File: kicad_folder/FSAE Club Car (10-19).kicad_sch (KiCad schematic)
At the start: 19 parts, among them J1 ECU PINOUT, K1 Shutdown Relay, K2 Main Relay, K3 Fuel pump and Injectors, K4 starter control relay, K5 starter solenoid, K6 Fans Relay, SW1 BOTS, SW2 cockpit Switch, SW3 Inertia Switch, SW4 Ignition, SW5 SW_Push

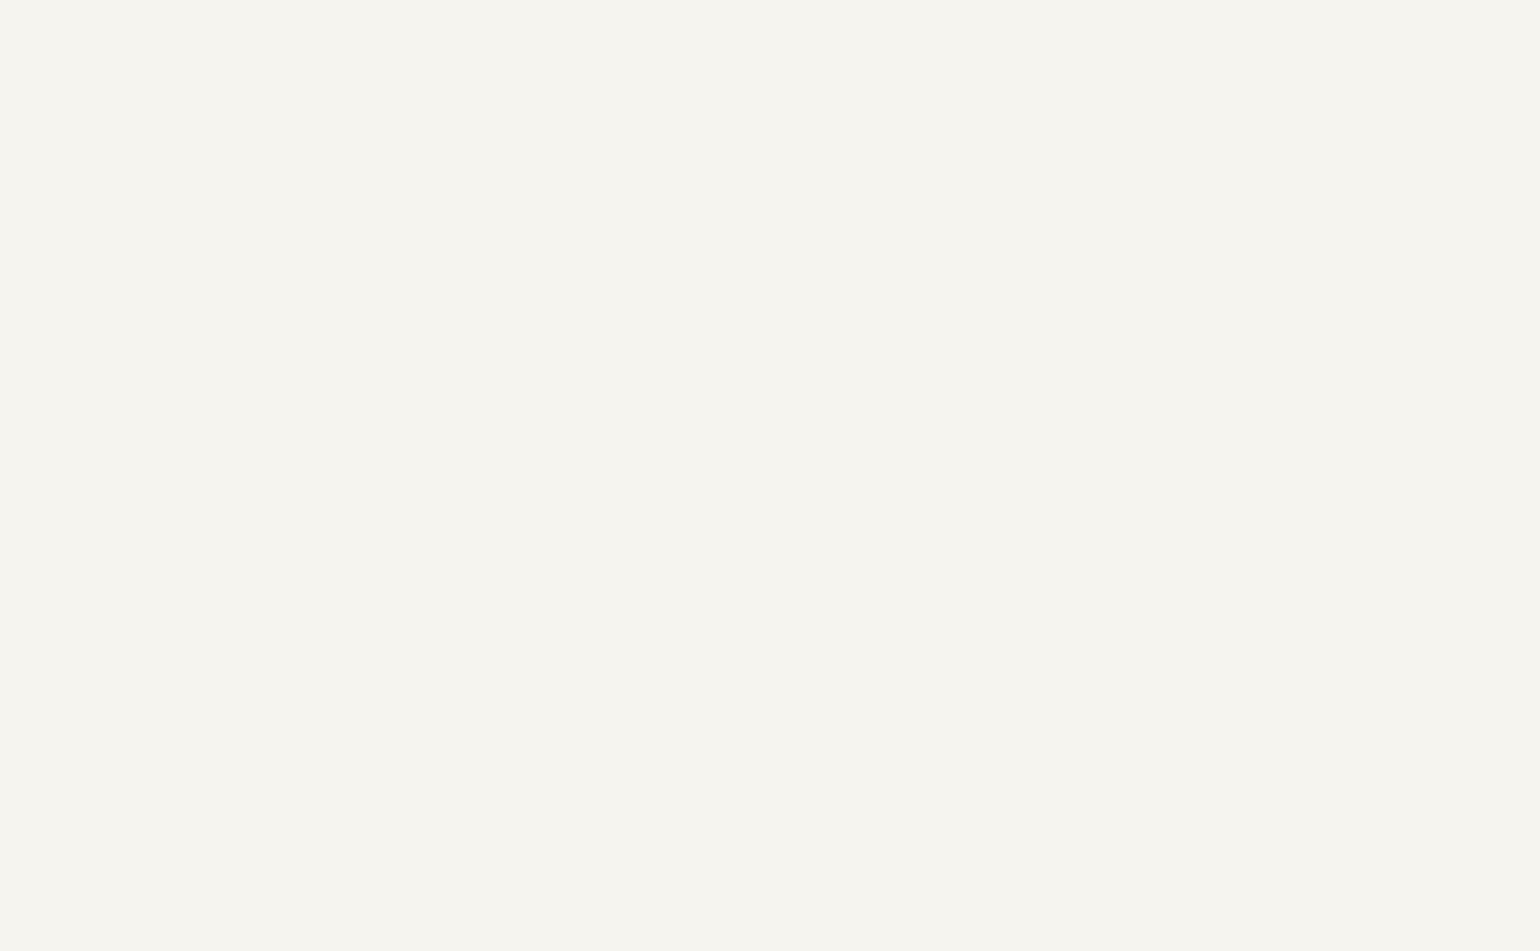
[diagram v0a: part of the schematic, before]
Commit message: redid diagram for clarity
- bots inertia switch and cockpit switch are now push open for accuracy
- starter is is now connected after ignition
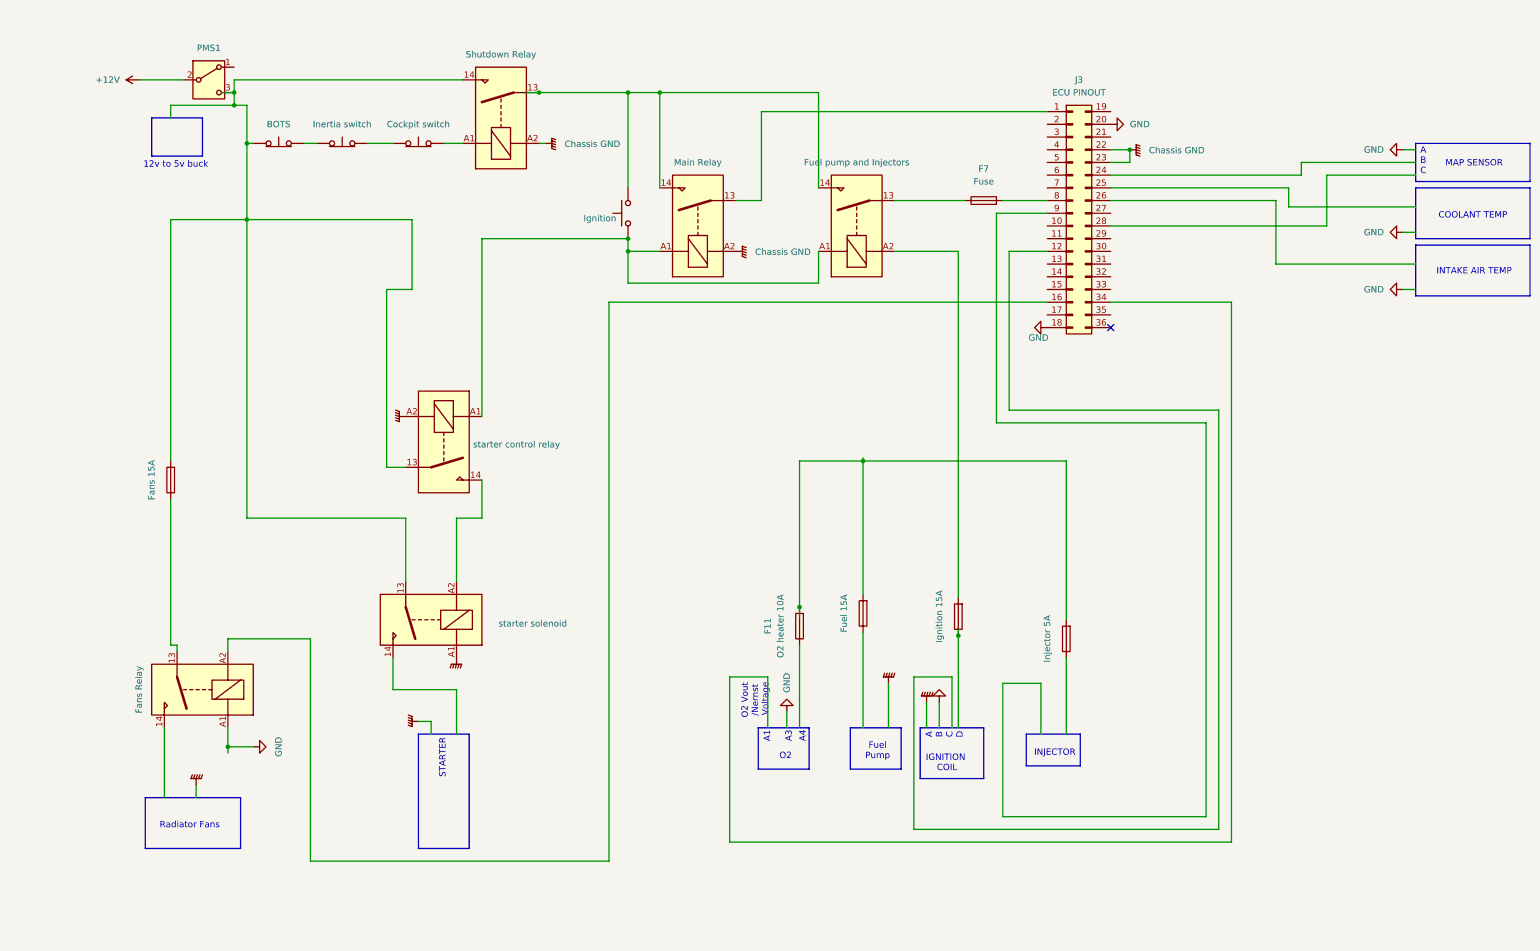
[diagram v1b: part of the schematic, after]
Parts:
- added F10: Injector 5A, symbol Device:Fuse
- added F11: O2 heater 10A, symbol Device:Fuse
- added F12: Fans 15A, symbol Device:Fuse
- added F7: Fuse, symbol Device:Fuse
- added F8: Fuel 15A, symbol Device:Fuse
- added F9: Ignition 15A, symbol Device:Fuse
- added J3: ECU PINOUT, symbol Connector_Generic:Conn_02x18_Top_Bottom
- added K10: starter control relay, Relay_THT:Relay_SPST-NO_Fujitsu_FTR-LYAA005x_FormA_Vertical, symbol Relay:Fujitsu_FTR-LYAA005x
- added K11: starter solenoid, Relay_THT:Relay_SPST-NO_Fujitsu_FTR-LYAA005x_FormA_Vertical, symbol Relay:Fujitsu_FTR-LYAA005x
- added K12: Fans Relay, Relay_THT:Relay_SPST-NO_Fujitsu_FTR-LYAA005x_FormA_Vertical, symbol Relay:Fujitsu_FTR-LYAA005x
- added K7: Shutdown Relay, Relay_THT:Relay_SPST-NO_Fujitsu_FTR-LYAA005x_FormA_Vertical, symbol Relay:Fujitsu_FTR-LYAA005x
- added K8: Main Relay, Relay_THT:Relay_SPST-NO_Fujitsu_FTR-LYAA005x_FormA_Vertical, symbol Relay:Fujitsu_FTR-LYAA005x
- added K9: Fuel pump and Injectors, Relay_THT:Relay_SPST-NO_Fujitsu_FTR-LYAA005x_FormA_Vertical, symbol Relay:Fujitsu_FTR-LYAA005x
- added PMS1: SW_SPDT, symbol Switch:SW_SPDT
- added SW10: BOTS, Button_Switch_SMD:Nidec_Copal_CAS-120A, symbol Switch:SW_Push_Open
- added SW11: Inertia switch, Button_Switch_SMD:Nidec_Copal_CAS-120A, symbol Switch:SW_Push_Open
- added SW12: Cockpit switch, Button_Switch_SMD:Nidec_Copal_CAS-120A, symbol Switch:SW_Push_Open
- added SW9: Ignition, symbol Switch:SW_Push
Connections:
- net +12V: now also PMS1.2 (B)
- net Chassis GND: now also J3.22 (Pin_22), J3.23 (Pin_23), K7.A2, K8.A2
- net GND: now also J3.18 (Pin_18), J3.20 (Pin_20), K12.A1
- net GNDPWR: now also K10.A2, K11.A1
- new net: J3.1 (Pin_1), K8.13
- new net: K7.13, K8.14, K9.14, SW9.2
- new net: K10.A1, K8.A1, K9.A1, SW9.1
- new net: J3.16 (Pin_16), K12.A2
- new net: F7.2, J3.8 (Pin_8)
- new net: F9.2, K9.A2
- new net: SW11.2 (B), SW12.1 (A)
- new net: K7.A1, SW12.2 (B)
- new net: F12.1, K12.13
- new net: F12.2, K10.13, K11.13, K7.14, PMS1.3 (C), SW10.1 (A)
- new net: K10.14, K11.A2
- new net: F10.2, F11.2, F8.2
- new net: F7.1, K9.13
- new net: SW10.2 (B), SW11.1 (A)
- no-connect marks 0 -> 1
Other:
- note added: "IGNITION COIL"
- note added: "O2 Vout /Nernst Voltage"

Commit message: stufff
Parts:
- added D1, D2, D3, D4, D5: D_Zener, Package_DIP:DIP-40_W15.24mm, symbol Device:D_Zener
- added SW13: starter, symbol Switch:SW_Push
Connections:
- net Chassis GND: now also D1.2 (A), D2.2 (A), D3.2 (A)
- net GNDPWR: now also D4.2 (A), D5.2 (A)
- net at K8.A1, K9.A1, SW9.1: now also D1.1 (K), D2.1 (K), SW13.2; no longer K10.A1
- net at J3.16 (Pin_16), K12.A2: now also D5.1 (K)
- net at F9.2: now also K9.13; no longer K9.A2
- net at K7.A1, SW12.2 (B): now also D3.1 (K)
- net at F7.1: now also K9.A2; no longer K9.13
- new net: D4.1 (K), K10.A1, SW13.1
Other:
- moved on the sheet: F11, F7

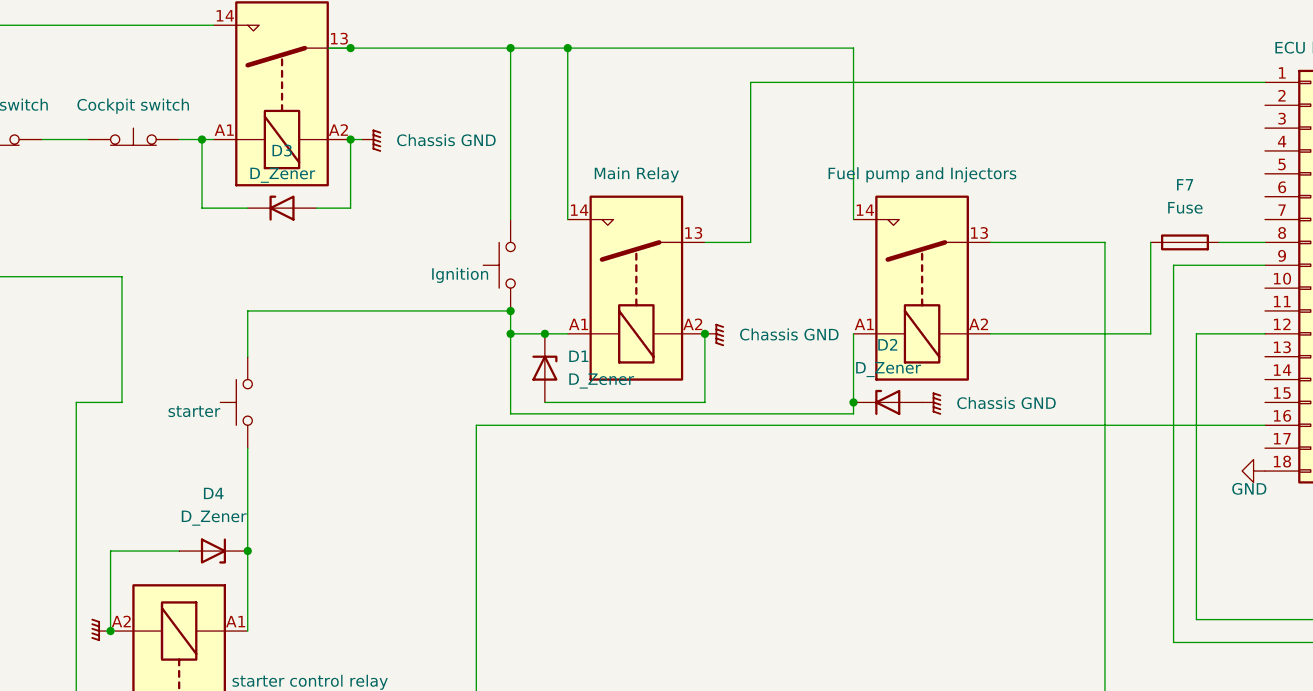
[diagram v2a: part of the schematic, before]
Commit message: zener sitde switch
i realized the Zener on the fuel pump relay was not actually protecting the ecu from the inductive flyback of the relay. so i switched which side its on . the fan relay does not have this problem as it is on the ecu side.
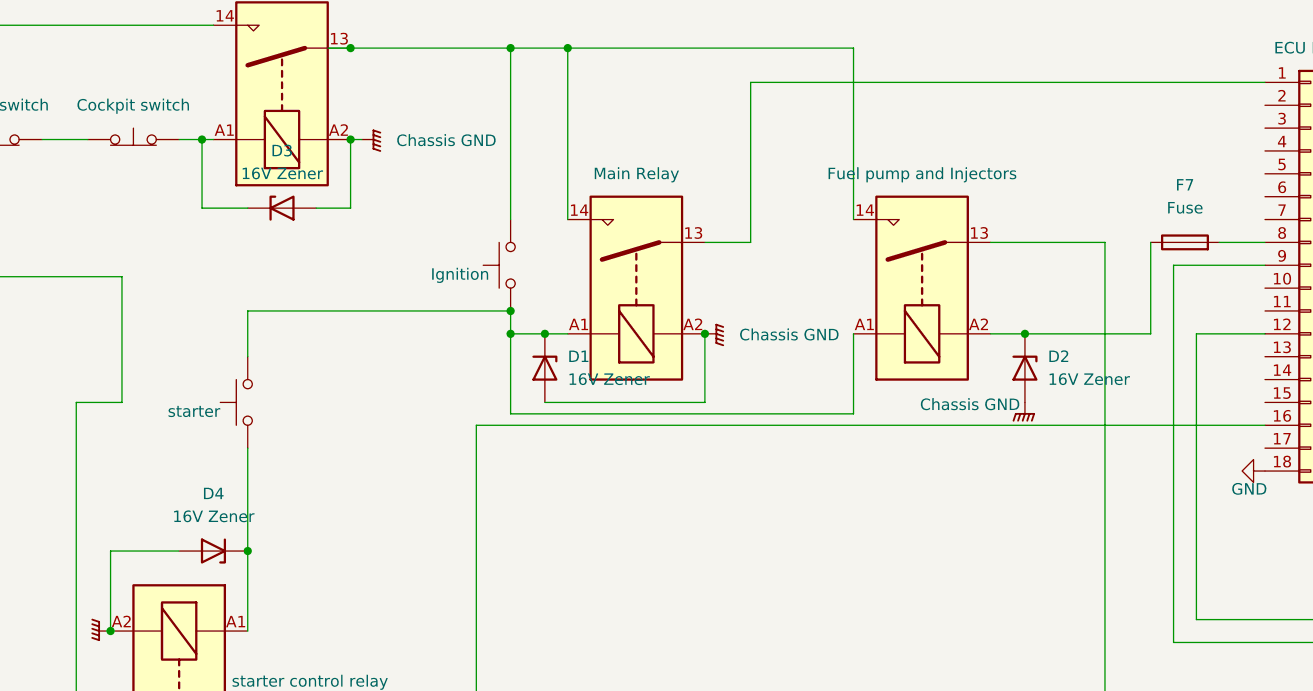
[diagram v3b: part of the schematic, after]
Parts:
- D1, D2, D3, D4: value D_Zener -> 16V Zener
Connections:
- net at D1.1 (K), K8.A1, K9.A1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: no longer D2.1 (K)
- net at F7.1, K9.A2: now also D2.1 (K)
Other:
- moved on the sheet: D2
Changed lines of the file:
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@@
 	)
 	(junction
-		(at 745.49 82.55)
+		(at 707.39 43.18)
 		(diameter 0)
 		(color 0 0 0 0)
 	)
 	(junction
-		(at 707.39 43.18)
+		(at 764.54 74.93)
 		(diameter 0)
 		(color 0 0 0 0)
@@
 	(wire
 		(pts
-			(xy 745.49 83.82) (xy 745.49 82.55)
-		)
-		(stroke
-			(width 0)
-			(type default)
-		)
-	)
-	(wire
-		(pts
 			(xy 257.81 40.64) (xy 257.81 43.18)
 		)
@@
 	(wire
 		(pts
+			(xy 760.73 74.93) (xy 764.54 74.93)
+		)
+		(stroke
+			(width 0)
+			(type default)
+		)
+	)
+	(wire
+		(pts
 			(xy 772.16 170.18) (xy 772.16 160.02)
 		)
@@
 	(wire
 		(pts
+			(xy 764.54 74.93) (xy 778.51 74.93)
+		)
+		(stroke
+			(width 0)
+			(type default)
+		)
+	)
+	(wire
+		(pts
 			(xy 864.87 77.47) (xy 836.93 77.47)
 		)
@@
 	(wire
 		(pts
-			(xy 778.51 74.93) (xy 760.73 74.93)
-		)
-		(stroke
-			(width 0)
-			(type default)
-		)
-	)
-	(wire
-		(pts
 			(xy 668.02 168.91) (xy 668.02 171.45)
 		)
@@
 	(wire
 		(pts
-			(xy 745.49 82.55) (xy 745.49 74.93)
+			(xy 745.49 74.93) (xy 745.49 83.82)
 		)
 		(stroke
@@
 			)
 		)
-		(property "Value" "D_Zener"
+		(property "Value" "16V Zener"
 			(at 674.37 95.25 0)
 			(show_name no)
@@
 	(symbol
 		(lib_id "Device:D_Zener")
-		(at 749.3 82.55 0)
+		(at 764.54 78.74 270)
 		(unit 1)
 		(body_style 1)
@@
 		(fields_autoplaced yes)
 		(property "Reference" "D2"
-			(at 749.3 76.2 0)
+			(at 767.08 77.4699 90)
 			(show_name no)
 			(do_not_autoplace no)
@@
 					(size 1.27 1.27)
 				)
+				(justify left)
 			)
 		)
-		(property "Value" "D_Zener"
-			(at 749.3 78.74 0)
+		(property "Value" "16V Zener"
+			(at 767.08 80.0099 90)
 			(show_name no)
 			(do_not_autoplace no)
@@
 					(size 1.27 1.27)
 				)
+				(justify left)
 			)
 		)
 		(property "Footprint" "Package_DIP:DIP-40_W15.24mm"
-			(at 749.3 82.55 0)
+			(at 764.54 78.74 0)
 			(hide yes)
 			(show_name no)
@@
 		)
 		(property "Datasheet" ""
-			(at 749.3 82.55 0)
+			(at 764.54 78.74 0)
 			(hide yes)
 			(show_name no)
@@
 		)
 		(property "Description" "Zener diode"
-			(at 749.3 82.55 0)
+			(at 764.54 78.74 0)
 			(hide yes)
 			(show_name no)
@@
 			)
 		)
-		(property "Value" "D_Zener"
+		(property "Value" "16V Zener"
 			(at 681.99 57.15 0)
 			(show_name no)
@@
 			)
 		)
-		(property "Value" "D_Zener"
+		(property "Value" "16V Zener"
 			(at 713.74 80.0099 90)
 			(show_name no)
@@
 	(symbol
 		(lib_id "power:GNDPWR")
-		(at 753.11 82.55 90)
+		(at 764.54 82.55 0)
 		(unit 1)
 		(body_style 1)
@@
 		(in_pos_files yes)
 		(dnp no)
-		(fields_autoplaced yes)
 		(property "Reference" "#PWR036"
-			(at 758.19 82.55 0)
+			(at 764.54 87.63 0)
 			(hide yes)
 			(show_name no)
@@
 		)
 		(property "Value" "Chassis GND"
-			(at 756.92 82.6769 90)
+			(at 758.444 82.804 0)
 			(show_name no)
 			(do_not_autoplace no)
@@
 					(size 1.27 1.27)
 				)
-				(justify right)
 			)
 		)
 		(property "Footprint" ""
-			(at 754.38 82.55 0)
+			(at 764.54 83.82 0)
 			(hide yes)
 			(show_name no)
@@
 		)
 		(property "Datasheet" ""
-			(at 754.38 82.55 0)
+			(at 764.54 83.82 0)
 			(hide yes)
 			(show_name no)
@@
 		)
 		(property "Description" "Power symbol creates a global label with name \"GNDPWR\" , global ground"
-			(at 753.11 82.55 0)
+			(at 764.54 82.55 0)
 			(hide yes)
 			(show_name no)

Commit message: new schematic
changed the common of starter control to recieve power from after the shutdown relay. same for fans relay

oh and theres a new maybe better schematic. ?
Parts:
- added D10: D_Zener, Package_DIP:DIP-40_W15.24mm, symbol Device:D_Zener
- added D14, D6, D7, D8: 16V Zener, Package_DIP:DIP-40_W15.24mm, symbol Device:D_Zener
- added F14: Fans 15A, symbol Device:Fuse
- added F19: Fuse, symbol Device:Fuse
- added F20: O2 heater 10A, symbol Device:Fuse
- added F21: Fuel 15A, symbol Device:Fuse
- added F22: Ignition 15A, symbol Device:Fuse
- added F23: Injector 5A, symbol Device:Fuse
- added J2: ECU PINOUT, symbol Connector_Generic_MountingPin:Conn_01x35_MountingPin
- added J4: Car_Side, symbol Connector_Generic_MountingPin:Conn_01x35_MountingPin
- added J5: Board_Side, symbol Connector_Generic_MountingPin:Conn_01x35_MountingPin
- added K13: Shutdown Relay, Relay_THT:Relay_SPST-NO_Fujitsu_FTR-LYAA005x_FormA_Vertical, symbol Relay:Fujitsu_FTR-LYAA005x
- added K14: Main Relay, Relay_THT:Relay_SPST-NO_Fujitsu_FTR-LYAA005x_FormA_Vertical, symbol Relay:Fujitsu_FTR-LYAA005x
- added K15: Fuel pump and Injectors, Relay_THT:Relay_SPST-NO_Fujitsu_FTR-LYAA005x_FormA_Vertical, symbol Relay:Fujitsu_FTR-LYAA005x
- added K16: starter solenoid, Relay_THT:Relay_SPST-NO_Fujitsu_FTR-LYAA005x_FormA_Vertical, symbol Relay:Fujitsu_FTR-LYAA005x
- added K18: starter control relay, Relay_THT:Relay_SPST-NO_Fujitsu_FTR-LYAA005x_FormA_Vertical, symbol Relay:Fujitsu_FTR-LYAA005x
- added K19: Fans Relay, Relay_THT:Relay_SPST-NO_Fujitsu_FTR-LYAA005x_FormA_Vertical, symbol Relay:Fujitsu_FTR-LYAA005x
- added PMS2: SW_SPDT, symbol Switch:SW_SPDT
- added SW14: BOTS, Button_Switch_SMD:Nidec_Copal_CAS-120A, symbol Switch:SW_Push_Open
- added SW15: Inertia switch, Button_Switch_SMD:Nidec_Copal_CAS-120A, symbol Switch:SW_Push_Open
- added SW16: Cockpit switch, Button_Switch_SMD:Nidec_Copal_CAS-120A, symbol Switch:SW_Push_Open
- added SW17: starter, symbol Switch:SW_Push
- added SW18: Ignition, symbol Switch:SW_Push
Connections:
- net +12V: now also PMS2.2 (B)
- net Chassis GND: now also D6.2 (A), D7.2 (A), D8.2 (A), J2.22 (Pin_22), J2.23 (Pin_23), K13.A2, K14.A2
- net GND: now also J2.18 (Pin_18), J4.20 (Pin_20), J5.20 (Pin_20), J5.21 (Pin_21), J5.22 (Pin_22), J5.23 (Pin_23), K19.A1
- net GNDPWR: now also D10.2 (A), D14.2 (A), K16.A1, K18.A2
- new net: SW15.2 (B), SW16.1 (A)
- new net: J4.2 (Pin_2), SW16.2 (B)
- new net: D14.1 (K), J5.6 (Pin_6), K18.A1
- new net: SW14.2 (B), SW15.1 (A)
- new net: F21.1, J5.9 (Pin_9)
- new net: F20.2, F21.2, F22.2, F23.2, K15.13
- new net: J4.1 (Pin_1), K16.13, PMS2.3 (C), SW14.1 (A)
- new net: J4.7 (Pin_7), K16.A2
- new net: F14.1, K19.13
- new net: J5.19 (Pin_19), K19.14
- new net: D10.1 (K), J2.16 (Pin_16), K19.A2
- new net: J4.3 (Pin_3), SW18.2
- new net: J4.4 (Pin_4), SW18.1
- new net: J4.5 (Pin_5), SW17.2
- new net: J4.6 (Pin_6), SW17.1
- new net: F14.2, J5.3 (Pin_3), K13.13, K14.14, K15.14
- new net: F20.1, J5.8 (Pin_8)
- new net: J5.1 (Pin_1), K13.14
- new net: D6.1 (K), J5.2 (Pin_2), K13.A1
- new net: D8.1 (K), F19.1, K15.A2
- new net: F19.2, J2.8 (Pin_8)
- new net: J2.1 (Pin_1), K14.13
- new net: J2.12 (Pin_12), J5.13 (Pin_13)
- new net: J2.24 (Pin_24), J5.15 (Pin_15)
- new net: J2.25 (Pin_25), J5.16 (Pin_16)
- new net: J2.26 (Pin_26), J5.17 (Pin_17)
- new net: J2.28 (Pin_28), J5.18 (Pin_18)
- new net: J2.34 (Pin_34), J5.12 (Pin_12)
- new net: J2.9 (Pin_9), J5.14 (Pin_14)
- new net: D7.1 (K), J5.4 (Pin_4), J5.5 (Pin_5), K14.A1, K15.A1, K18.13
- new net: J5.7 (Pin_7), K18.14
- new net: F23.1, J5.11 (Pin_11)
- new net: F22.1, J5.10 (Pin_10)
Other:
- note added: "Coolant_Temp"
- note added: "Fuel_pump"
- note added: "Ignition+"
- note added: "Ignition-"
- note added: "Ignition_coil+"
- note added: "Ignition_coil-"
- note added: "Injector+"
- note added: "Injector-"
- note added: "Intake_Air_Temp"
- note added: "Kill_Switches"
- note added: "MAP_A"
- note added: "MAP_B"
- note added: "O2_Heater"
- note added: "O2_V_out_Nernst"
- note added: "Rad_Fan"
- note added: "Starter"
- note added: "Starter_Switch+"
- note added: "Starter_Switch-"
- note added: "V_in"

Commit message: LABELS
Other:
- note added: "RAD_FAN"
- note added: "Sens_GND"
- note removed: "Rad_Fan"
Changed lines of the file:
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@@
+		)
+	)
+	(text "Sens_GND"
+		(exclude_from_sim no)
+		(at 204.216 347.472 0)
+		(effects
+			(font
+				(size 1.27 1.27)
+			)
 		)
 	)
@@
 		)
 	)
-	(text "Rad_Fan"
+	(text "RAD_FAN"
 		(exclude_from_sim no)
 		(at 204.216 344.424 0)
@@
 		)
 	)
+	(text "Sens_GND"
+		(exclude_from_sim no)
+		(at 204.216 354.838 0)
+		(effects
+			(font
+				(size 1.27 1.27)
+			)
+		)
+	)
+	(text "Sens_GND"
+		(exclude_from_sim no)
+		(at 204.0103 350.012 0)
+		(effects
+			(font
+				(size 1.27 1.27)
+			)
+		)
+	)
 	(text "MAP_B"
 		(exclude_from_sim no)
@@
 		(effects
 			(font
+				(size 1.27 1.27)
+			)
+		)
+	)
+	(text "Sens_GND"
+		(exclude_from_sim no)
+		(at 203.962 352.298 0)
+		(effects
+			(font
